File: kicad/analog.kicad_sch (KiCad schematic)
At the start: 17 parts, among them J25 pH probe, J26 AIN, U5 ADS1115IDGSR, U6 TLV9062IDR

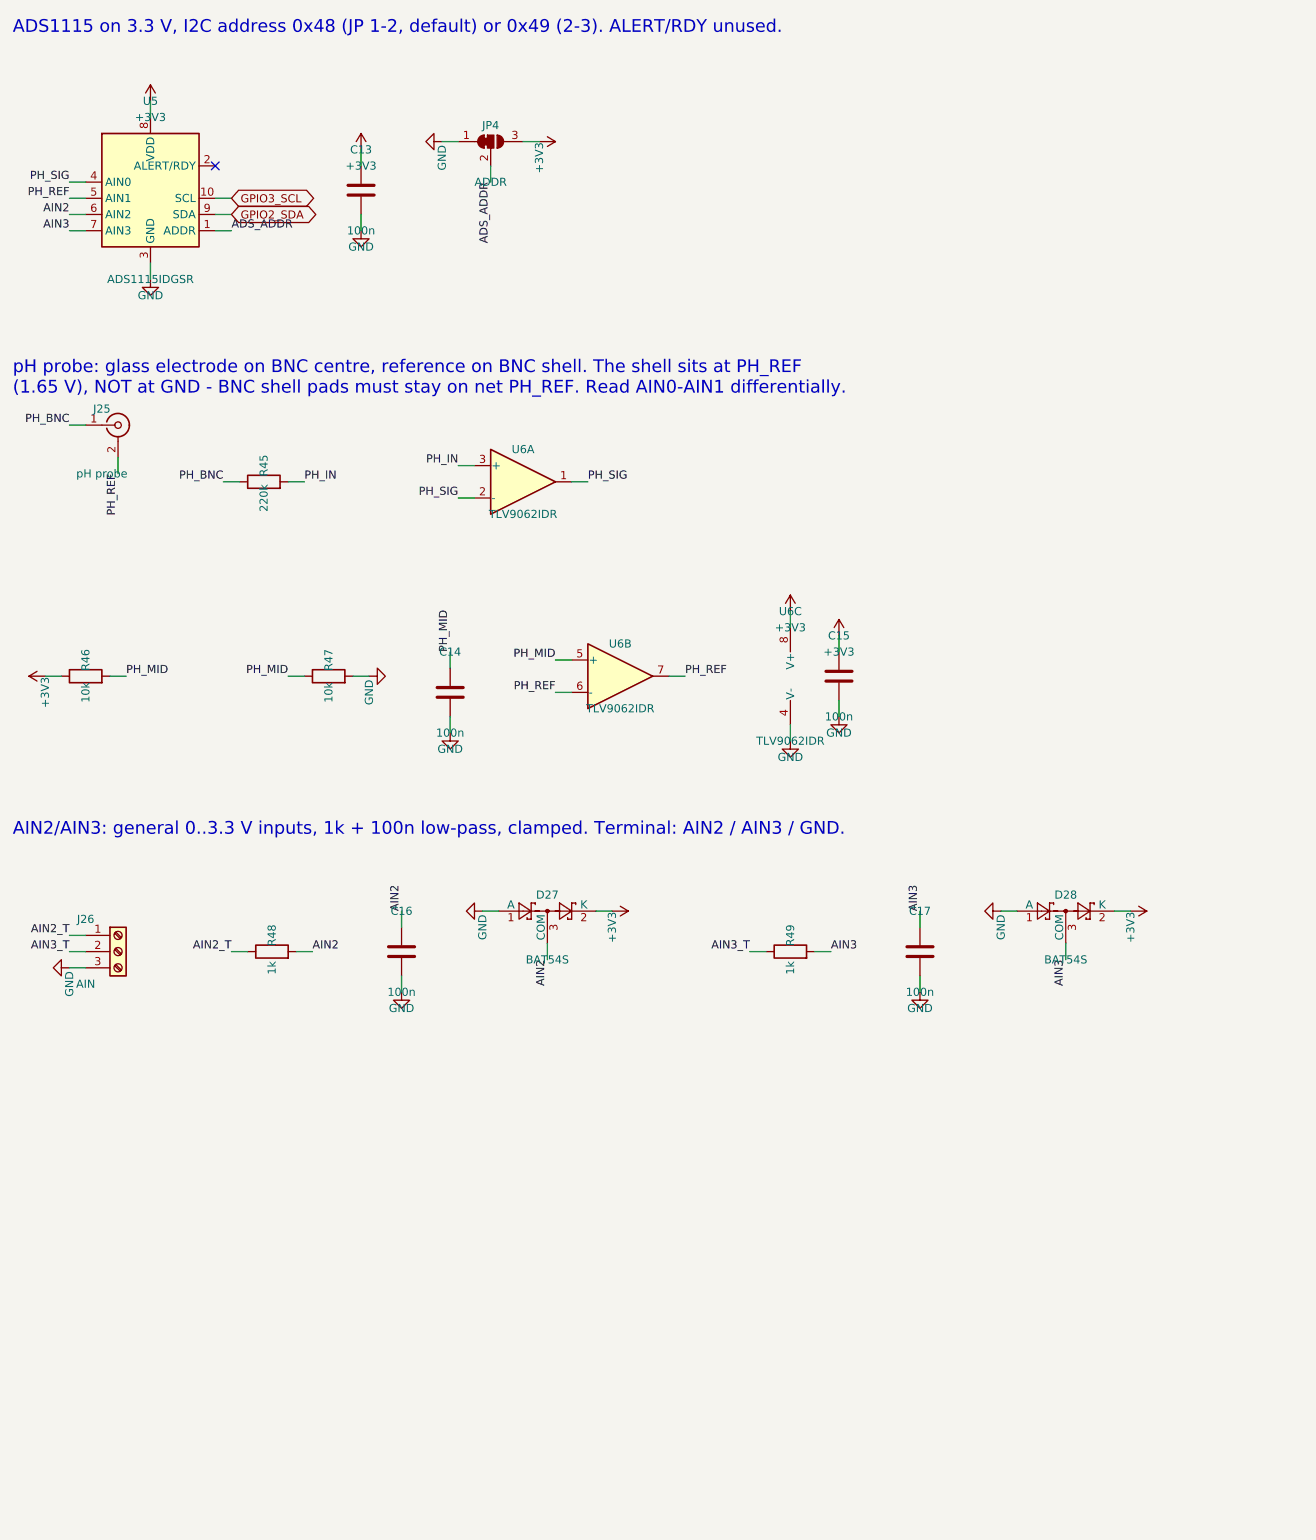
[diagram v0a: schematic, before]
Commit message: kicad: single-ended pH front end, input for external pH module
aquaPi's ADS1115 driver reads single-ended only. Bias the probe
reference from a TL431 (PH_REF = 1.25 V) so AIN0 works single-ended
with the offset removed by 2-point calibration; keep PH_REF on AIN1 for
a later differential mode. Add 50 Hz filtering (1 nF input, 10k/10u
after the buffer) and a +5V/SIG/GND terminal on AIN2 for the common
pH amplifier modules. BOM and README updated.

Co-Authored-By: Claude Opus 5.5 <noreply@anthropic.com>
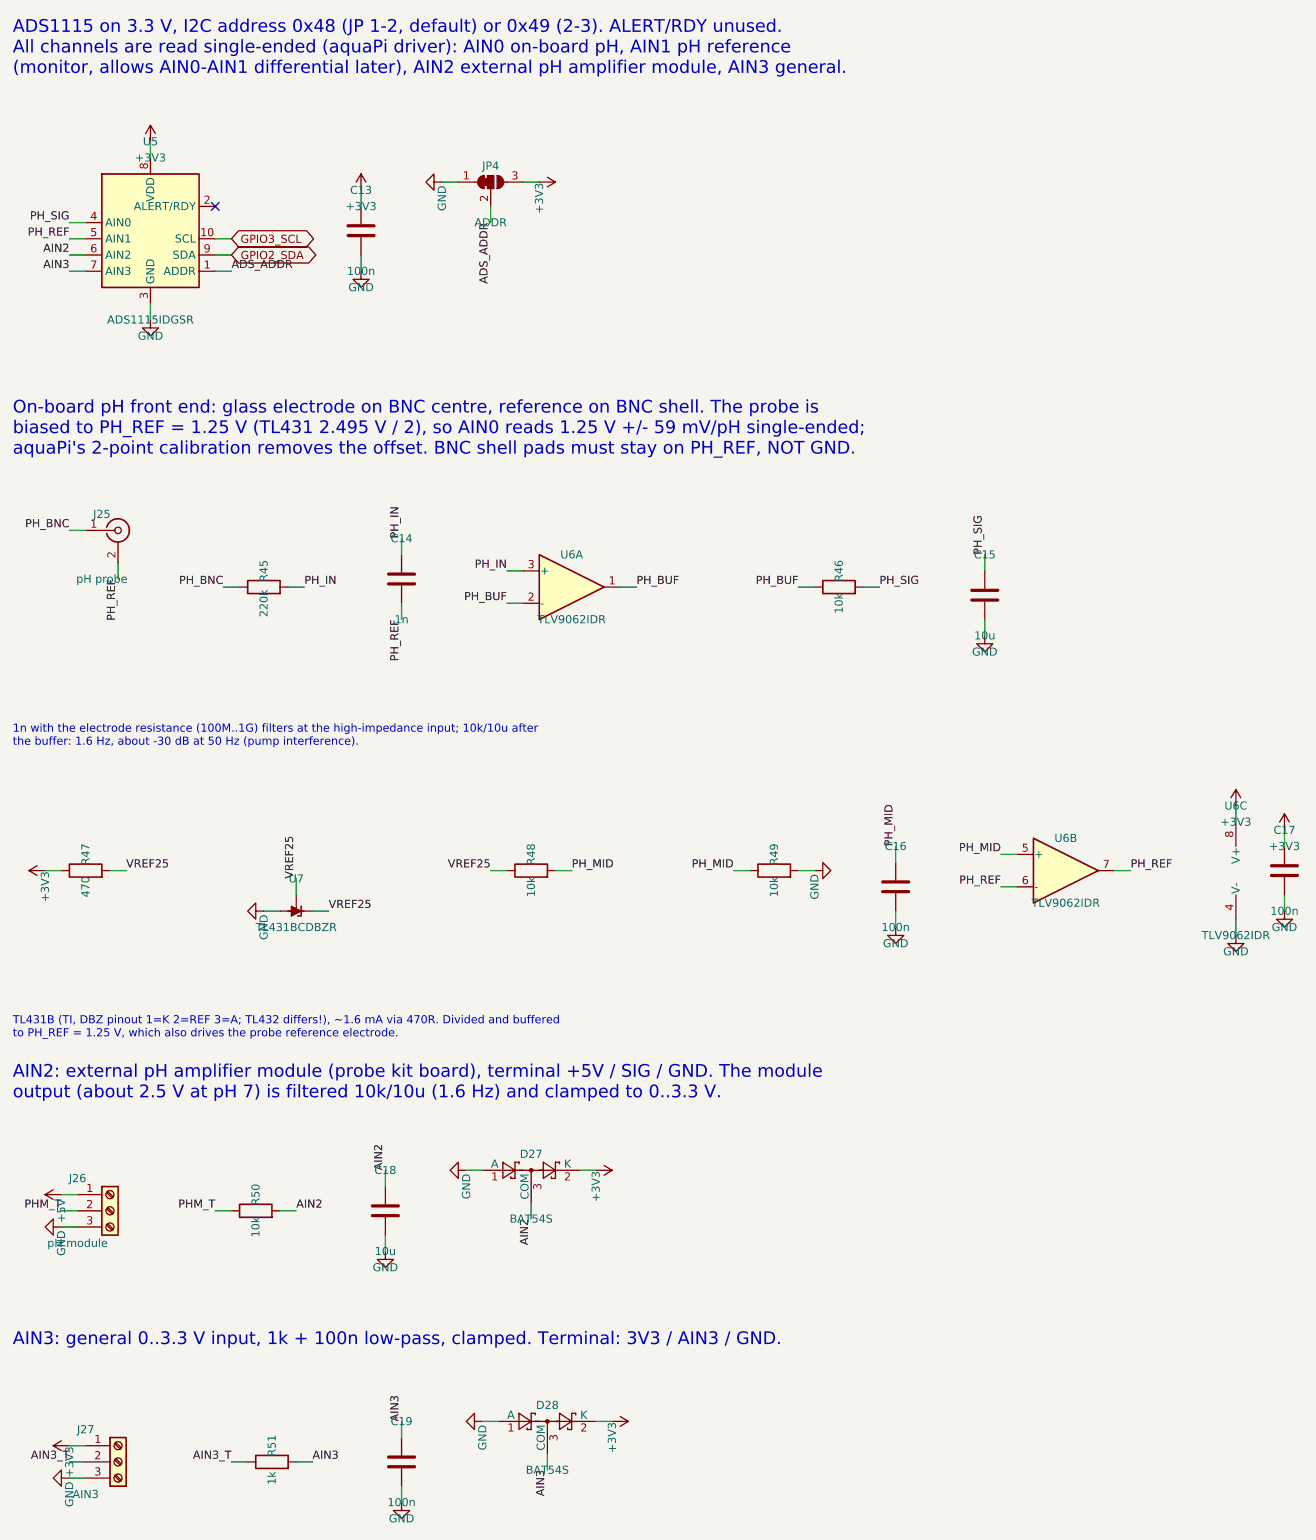
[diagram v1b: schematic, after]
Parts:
- added C18: 10u, Capacitor_SMD:C_0805_2012Metric, symbol Device:C
- added C19: 100n, Capacitor_SMD:C_0805_2012Metric, symbol Device:C
- added J27: AIN3, TerminalBlock_Phoenix:TerminalBlock_Phoenix_MKDS-1,5-3-5.08_1x03_P5.08mm_Horizontal, symbol Connector:Screw_Terminal_01x03
- added R50: 10k, Resistor_SMD:R_0805_2012Metric, symbol Device:R
- added R51: 1k, Resistor_SMD:R_0805_2012Metric, symbol Device:R
- added U7: TL431BCDBZR, Package_TO_SOT_SMD:SOT-23, symbol Reference_Voltage:TL431DBZ
- C14: value 100n -> 1n; LCSC C49678 -> C46653
- C15: value 100n -> 10u; LCSC C49678 -> C15850
- J26: value AIN -> pH module
- R47: value 10k -> 470; LCSC C17414 -> C17710
- R48, R49: value 1k -> 10k; LCSC C17513 -> C17414
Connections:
- net +3V3: now also C17.1, R47.1, J27.1 (Pin_1); no longer C15.1, R46.1
- net AIN2: now also C18.1, R50.2; no longer C16.1, R48.2
- net AIN3: now also C19.1, R51.2; no longer C17.1, R49.2
- net AIN3_T: now also J27.2 (Pin_2), R51.1; no longer J26.2 (Pin_2), R49.1
- net GND: now also R49.2, C18.2, C19.2, J27.3 (Pin_3), U7.3 (A); no longer C14.2, R47.2
- net PH_IN: now also C14.1
- net PH_MID: now also C16.1, R48.2, R49.1; no longer C14.1, R46.2, R47.1
- net PH_REF: now also C14.2
- net PH_SIG: now also C15.1, R46.2; no longer U6.1, U6.2 (-)
- net AIN2_T renamed +5V
- net +5V: no longer R48.1
- new net PHM_T: J26.2 (Pin_2), R50.1
- new net PH_BUF: R46.1, U6.1, U6.2 (-)
- new net VREF25: R47.2, R48.1, U7.1 (K), U7.2 (REF)
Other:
- note added: "1n with the electrode resistance (100M..1G) filters at the high-impedance input; 10k/10u after the buffer: 1.6 Hz, about -30 dB at 50 Hz (pump interference)."
- note added: "ADS1115 on 3.3 V, I2C address 0x48 (JP 1-2, default) or 0x49 (2-3). ALERT/RDY unused. All channels are read single-ended (aquaPi driver): AIN0 on-board pH, AIN1 pH reference (monitor, allows AIN0-AIN1 differential later), AIN2 external pH amplifier module, AIN3 general."
- note added: "AIN2: external pH amplifier module (probe kit board), terminal +5V / SIG / GND. The module output (about 2.5 V at pH 7) is filtered 10k/10u (1.6 Hz) and clamped to 0..3.3 V."
- note added: "AIN3: general 0..3.3 V input, 1k + 100n low-pass, clamped. Terminal: 3V3 / AIN3 / GND."
- note added: "On-board pH front end: glass electrode on BNC centre, reference on BNC shell. The probe is biased to PH_REF = 1.25 V (TL431 2.495 V / 2), so AIN0 reads 1.25 V +/- 59 mV/pH single-ended; aquaPi's 2-point calibration removes the offset. BNC shell pads must stay on PH_REF, NOT GND."
- note added: "TL431B (TI, DBZ pinout 1=K 2=REF 3=A; TL432 differs!), ~1.6 mA via 470R. Divided and buffered to PH_REF = 1.25 V, which also drives the probe reference electrode."
- note removed: "ADS1115 on 3.3 V, I2C address 0x48 (JP 1-2, default) or 0x49 (2-3). ALERT/RDY unused."
- note removed: "AIN2/AIN3: general 0..3.3 V inputs, 1k + 100n low-pass, clamped. Terminal: AIN2 / AIN3 / GND."
- note removed: "pH probe: glass electrode on BNC centre, reference on BNC shell. The shell sits at PH_REF (1.65 V), NOT at GND - BNC shell pads must stay on net PH_REF. Read AIN0-AIN1 differentially."

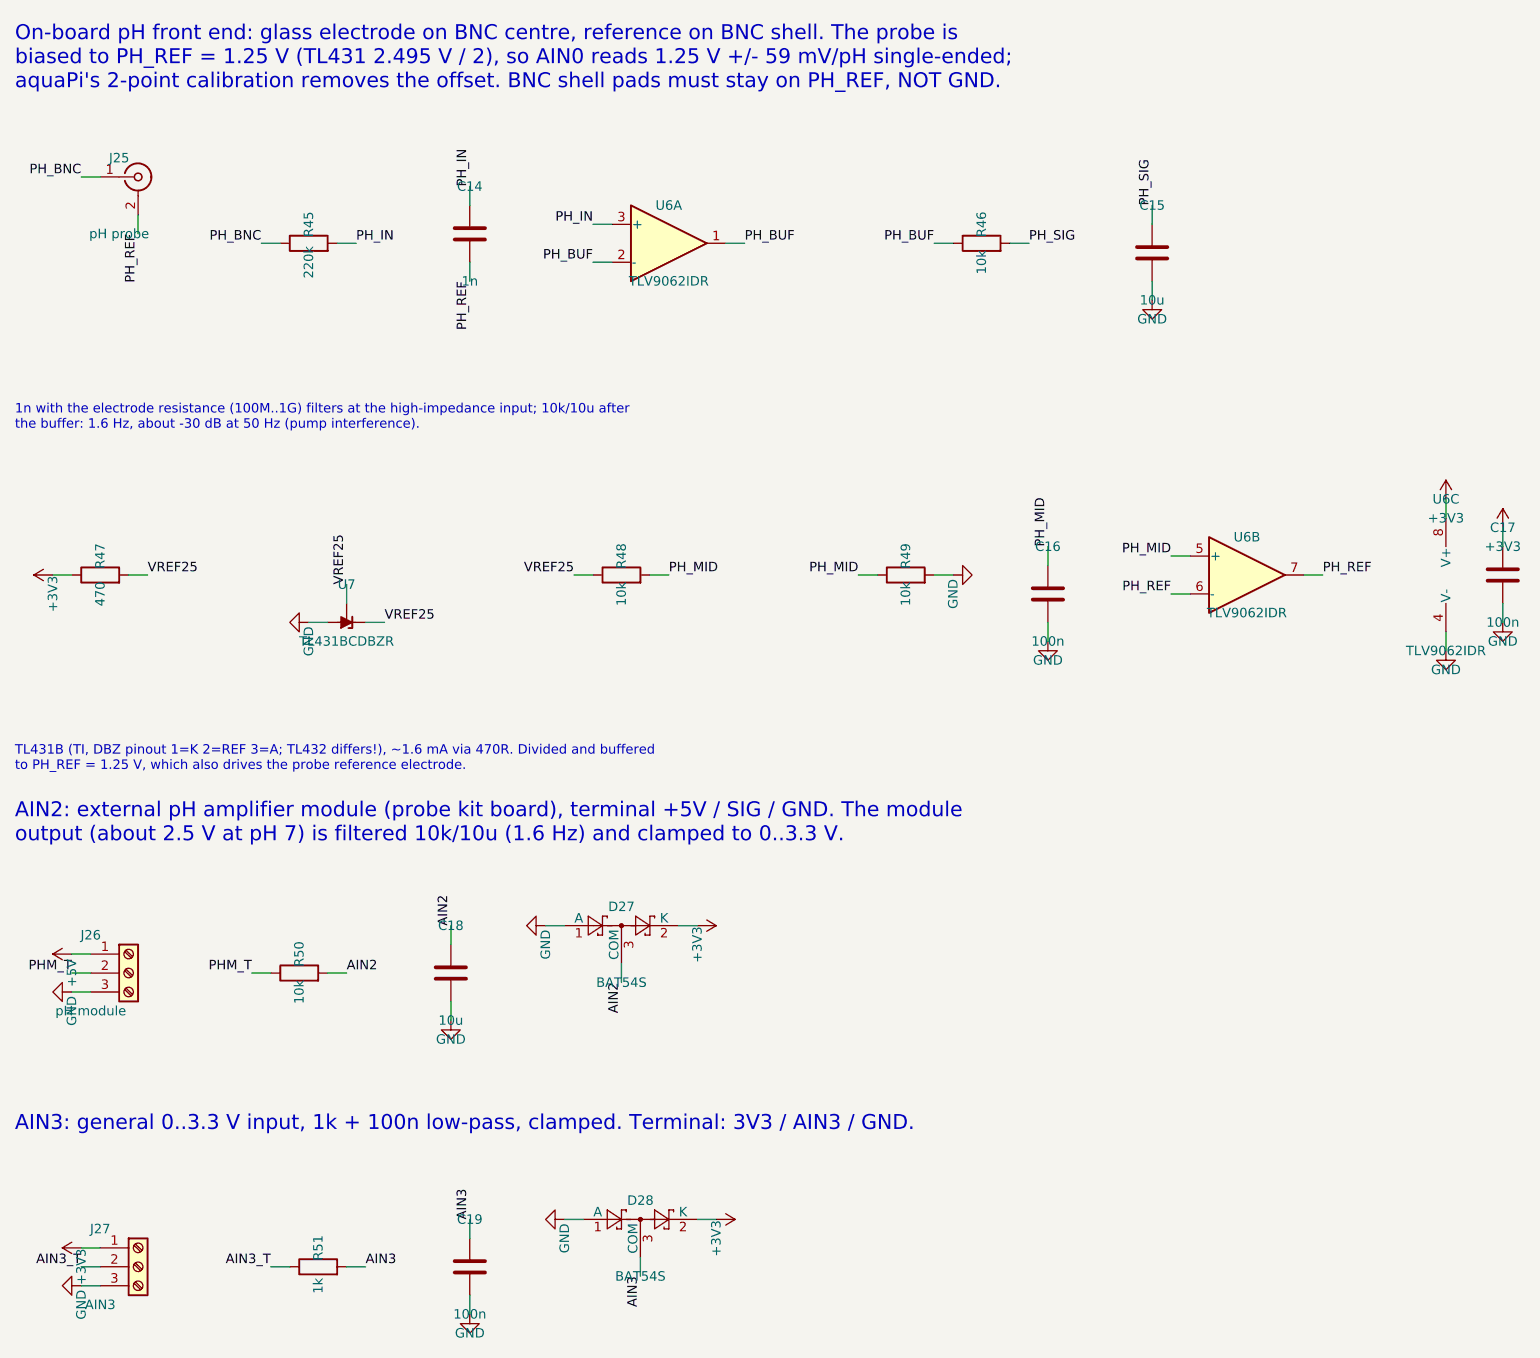
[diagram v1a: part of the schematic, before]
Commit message: kicad: minimise pH probe load, drop input capacitor
The 1 nF on the high-impedance pH input had an insulation resistance
(MLCC spec ~10 GOhm) far below the op-amp input (0.5 pA typ), so it
dominated the probe load. The probe now only sees the TLV9062 input;
50 Hz filtering stays after the buffer. Layout note: guard ring driven
by PH_BUF around the input.

Co-Authored-By: Claude Opus 5.5 <noreply@anthropic.com>
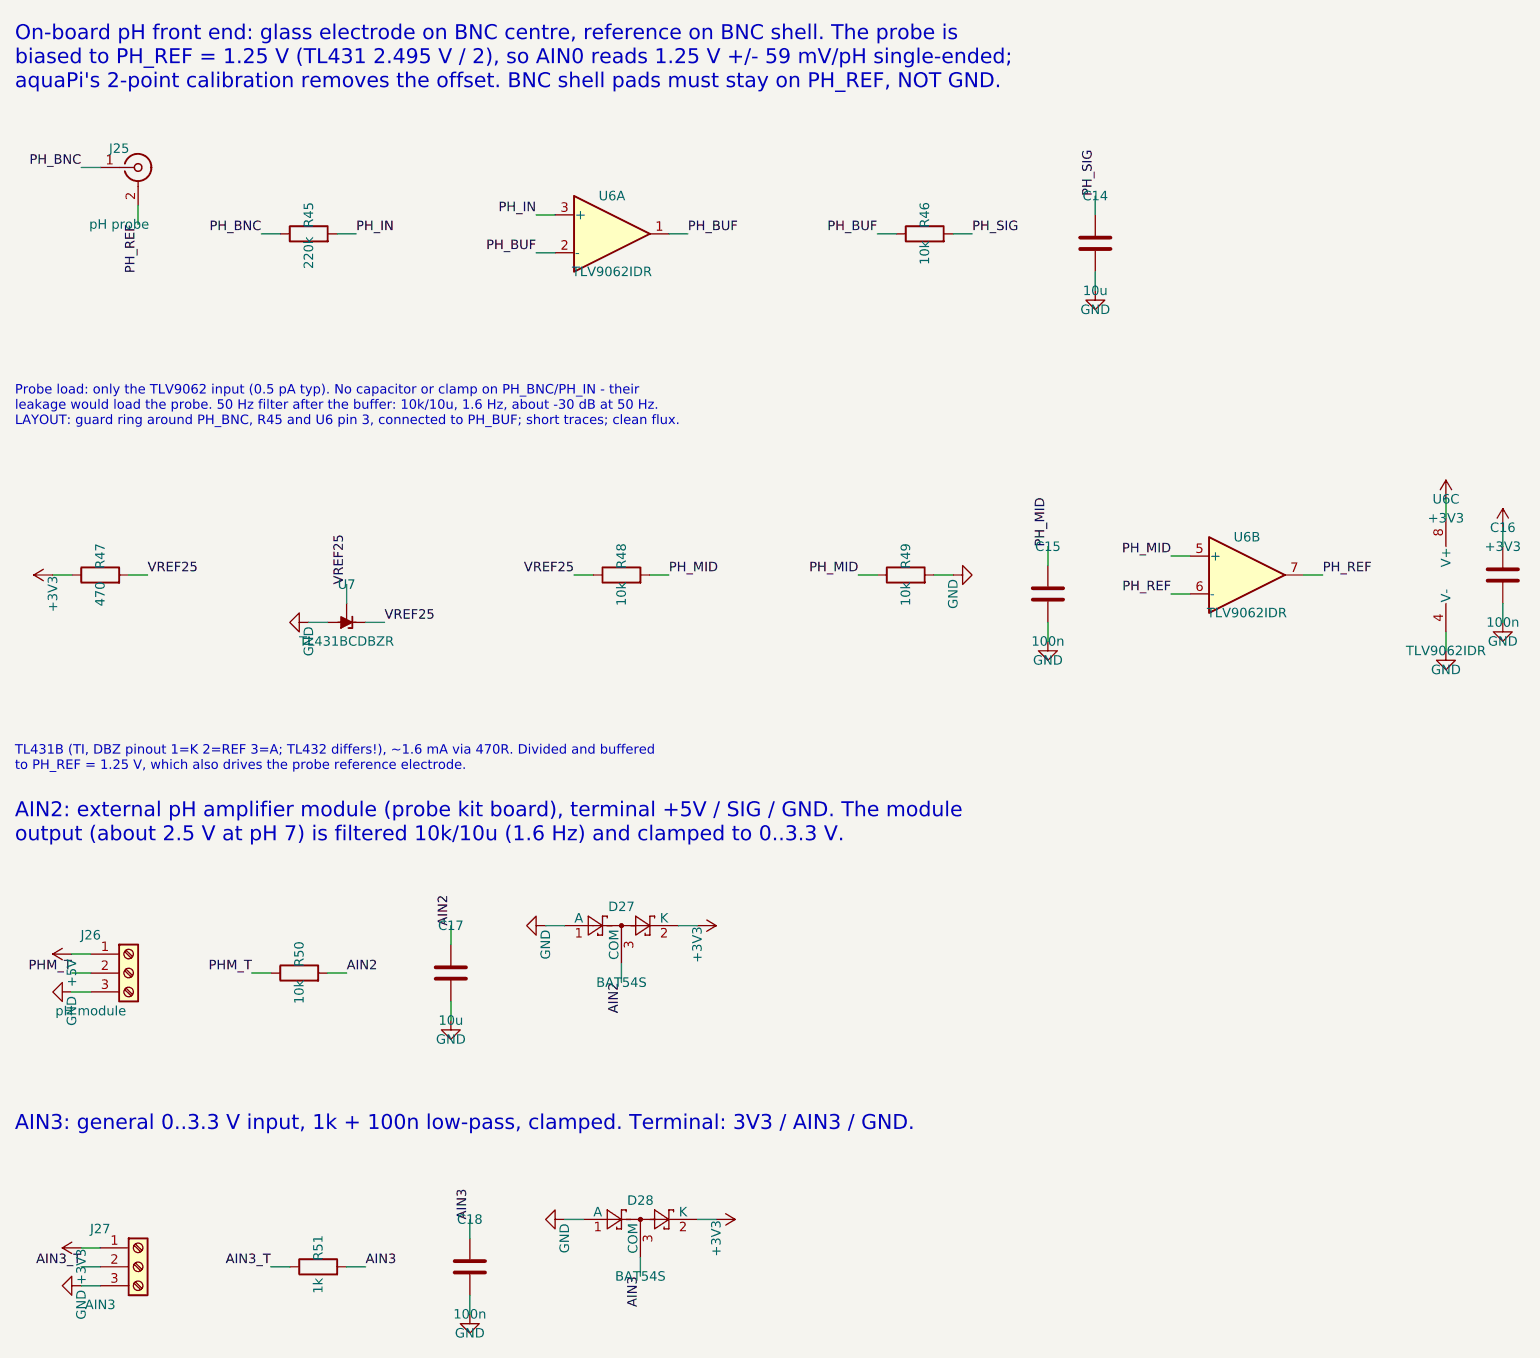
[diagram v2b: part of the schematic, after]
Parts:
- removed C19: 100n, Capacitor_SMD:C_0805_2012Metric, symbol Device:C
- C14: value 1n -> 10u; LCSC C46653 -> C15850
- C15, C18: value 10u -> 100n; LCSC C15850 -> C49678
- C17: value 100n -> 10u; LCSC C49678 -> C15850
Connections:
- net +3V3: now also C16.1; no longer C17.1
- net AIN2: now also C17.1; no longer C18.1
- net AIN3: now also C18.1
- net GND: now also C14.2
- net PH_IN: no longer C14.1
- net PH_MID: now also C15.1; no longer C16.1
- net PH_REF: no longer C14.2
- net PH_SIG: now also C14.1; no longer C15.1
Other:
- note added: "Probe load: only the TLV9062 input (0.5 pA typ). No capacitor or clamp on PH_BNC/PH_IN - their leakage would load the probe. 50 Hz filter after the buffer: 10k/10u, 1.6 Hz, about -30 dB at 50 Hz. LAYOUT: guard ring around PH_BNC, R45 and U6 pin 3, connected to PH_BUF; short traces; clean flux."
- note removed: "1n with the electrode resistance (100M..1G) filters at the high-impedance input; 10k/10u after the buffer: 1.6 Hz, about -30 dB at 50 Hz (pump interference)."
